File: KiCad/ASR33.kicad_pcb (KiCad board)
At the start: 2 copper layers, 42 x 35 mm, 34 parts, among them J1 USB-C, J2 Start, J3 Control, J4 Tx/Rx, U1 ESP32-WROOM-32, U2 FT231XQ, U3 NCR402U, U4 NCR402U, U5 NX6020CAKS, U6 LMR16006+FB

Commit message: Reworked
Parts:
- removed J4: Tx/Rx, RevK:Molex_MiniSPOX_H4RA
- removed the R9 at (134.6, 129.3)
- removed the U5 at (134.6, 132.0)
- added C5: NF, RevK:C_0603, F.Cu at (145.0, 132.0)
- added Q1: NX7002AK, Package_TO_SOT_SMD:SOT-23, F.Cu at (140.5, 132.0)
- added U6: QR, RevK:QR-ASR33, B.Cu at (123.0, 113.0)
- J2: value Start -> Control; footprint RevK:Molex_MiniSPOX_H2RA -> RevK:Molex_MiniSPOX_H3RA
- J3: value Control -> Teletype; footprint RevK:Molex_MiniSPOX_H3RA -> RevK:Molex_MiniSPOX_H6RA
- moved U4 7.40 mm to (131.0, 132.0)
- moved J3 6.35 mm to (141.2, 136.4)
- moved D2 4.20 mm to (152.0, 132.0)
- moved U3 4.20 mm to (135.0, 132.0)
- moved D3 4.00 mm to (148.0, 132.0)
- moved R9 2.00 mm to (143.4, 132.0), turned to 90 degrees
- moved J2 1.30 mm to (155.0, 136.4)
- renumbered C5 to C6, C6 to C7, C7 to C8, R11 to R9, U6 to U5
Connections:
- D2 pad 3: MOTOR -> POWER
- D2 pad 6: POWER -> MOTOR
- D3 pad 3: RX20MA -> START
- D3 pad 6: START -> RX20MA
- J2 pad 2: START -> POWER
- J3 pad 2: POWER -> START
- J3 pad 3: MOTOR -> Net-(J3-Pad3)
- U1 pad 23: unconnected-(U1-Pad23) -> USB
- U1 pad 24: unconnected-(U1-Pad24) -> CHARGER
- U1 pad 26: TX20MA -> START
- U1 pad 27: RX20MA -> TX20MA
- U1 pad 28: USB -> RX20MA
- U1 pad 29: CHARGER -> unconnected-(U1-Pad29)
- U1 pad 30: MOTOR -> unconnected-(U1-Pad30)
- U1 pad 31: POWER -> unconnected-(U1-Pad31)
- U1 pad 36: unconnected-(U1-Pad36) -> POWER
- U1 pad 37: START -> MOTOR
- U3 pad 2: Net-(R9-Pad1) -> Net-(J3-Pad3)
- U3 pad 3: Net-(R9-Pad1) -> Net-(J3-Pad3)
- U3 pad 5: Net-(R9-Pad1) -> Net-(J3-Pad3)
- U4 pad 2: Net-(J4-Pad4) -> Net-(J3-Pad5)
- U4 pad 3: Net-(J4-Pad4) -> Net-(J3-Pad5)
- U4 pad 5: Net-(J4-Pad4) -> Net-(J3-Pad5)
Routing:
- net Net-(J3-Pad5): track 0.00 -> 24.3 mm
- net Net-(J3-Pad3): track 0.00 -> 14.9 mm
- net Net-(J4-Pad4): track 12.4 -> 0.00 mm
- net MOTOR: track 26.7 -> 15.0 mm
- net START: track 15.0 -> 25.2 mm
- net Net-(R9-Pad1): track 9.04 -> 0.00 mm
- net CHARGER: track 16.1 -> 8.31 mm, vias 2 -> 0
- net GND: track 17.5 -> 22.7 mm, vias 9 -> 8
- net Net-(J3-Pad4): track 0.00 -> 5.03 mm
- net USB: track 14.1 -> 9.14 mm, vias 2 -> 0
- net TX20MA: track 9.33 -> 5.21 mm
- net Net-(J4-Pad2): track 3.96 -> 0.00 mm
- net GPIO0: track 14.7 -> 17.2 mm
- net Net-(R9-Pad2): track 2.28 -> 0.00 mm
- net +3V3: track 75.0 -> 76.8 mm, vias 4 -> 5
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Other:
- board text added: "MTR"
- board text added: "PWR"
- board text added: "RUN"
- board text added: "RX<"
- board text added: "RX>"
- board text added: "TX<"
- board text added: "TX>"
- board text removed: "+"
- board text removed: "-"
- board text removed: "Motor"
- board text removed: "Power"
- board text removed: "Rx"
- board text removed: "Start"
- board text removed: "Tx"

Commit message: Tweak, added button
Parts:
- added SW1: SW_Push, RevK:SW_PUSH_6mm_PTH, F.Cu at (130.5, 117.3)
- moved R10 3.00 mm to (119.0, 125.1)
- moved R8 3.00 mm to (119.0, 122.0)
- moved U5 0.78 mm to (121.8, 119.8)
- moved R9 0.30 mm to (143.7, 132.0)
- moved C5 0.20 mm to (145.2, 132.0)
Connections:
- U1 pad 16: unconnected-(U1-Pad16) -> BUTTON
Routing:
- net BUTTON: track 0.00 -> 10.8 mm
- net +3V3: track 76.8 -> 86.2 mm, vias 5 -> 4
- net O: track 27.6 -> 30.1 mm
- net EN: track 36.1 -> 38.2 mm
- net GPIO0: track 17.2 -> 18.9 mm
- net Net-(R10-Pad2): track 3.61 -> 4.71 mm
- net I: track 23.4 -> 24.1 mm
- net RX20MA: track 27.0 -> 27.6 mm
- net USB: track 9.14 -> 8.64 mm
- net GND: track 22.7 -> 22.8 mm, vias 8 -> 7
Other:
- board text added: "Power 3.3V"
- board text added: "Teletype 20mA"
- board text added: "USB-C"

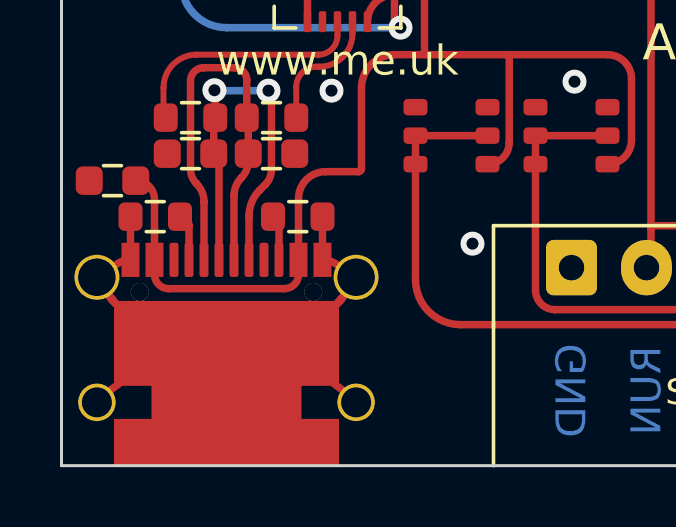
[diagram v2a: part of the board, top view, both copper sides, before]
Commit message: Correct pos for regulator
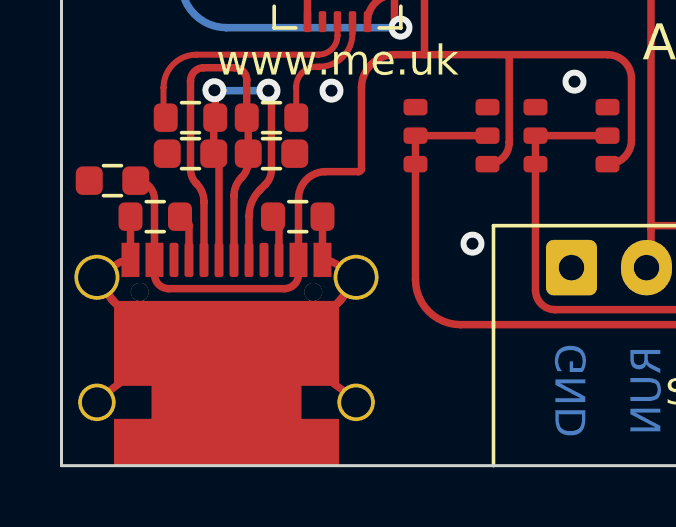
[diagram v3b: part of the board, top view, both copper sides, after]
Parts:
- moved D4 0.79 mm to (125.0, 117.5)
- moved C6 0.79 mm to (122.0, 121.9)
- moved C8 0.78 mm to (125.3, 114.4)
- moved L1 0.78 mm to (121.8, 115.9)
- moved C7 0.77 mm to (125.3, 120.7)
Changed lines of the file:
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@@
       (primitives
     (gr_arc (start 2.89 -3.045) (mid 0 -0.155) (end -2.89 -3.045) (width 0.25))
-    (gr_arc (start 4.294753 -3.49127) (mid -0.020907 -1.02625) (end -4.315692 -3.527464) (width 0.25))
+    (gr_arc (start 4.294753 -3.49127) (mid -0.016568 -1.026234) (end -4.311371 -3.519937) (width 0.25))
     (gr_arc (start -3.2 -2.485) (mid -4.015 -3.3) (end -3.2 -4.115) (width 0.25))
     (gr_arc (start 3.2 -4.115) (mid 4.015 -3.3) (end 3.2 -2.485) (width 0.25))
-    (gr_arc (start -4.32 0.635) (mid 0 -1.154403) (end 4.32 0.635) (width 0.25))
+    (gr_arc (start -4.32 0.635) (mid -0.000001 -1.154403) (end 4.319999 0.634999) (width 0.25))
         (gr_poly (pts
             (xy 3.75 0.085)
@@
   )
   (footprint "RevK:Hidden" (layer "F.Cu")
-    (at 125.95 121.14 180)
+    (at 125.35 120.65 180)
     (property "Note" "0603 or 0805")
     (property "Part No" "")
@@
   )
   (footprint "RevK:Hidden" (layer "F.Cu")
-    (at 125.95 114.9 180)
+    (at 125.35 114.4 180)
     (property "Note" "0603 or 0805")
     (property "Part No" "")
@@
   )
   (footprint "RevK:Hidden" (layer "F.Cu")
-    (at 125.57 118.02 90)
+    (at 124.96 117.52 90)
     (property "Manufacturer" "Bourns")
     (property "Note" "")
@@
   )
   (footprint "RevK:Hidden" (layer "F.Cu")
-    (at 122.4 116.4 90)
+    (at 121.8 115.9 90)
     (property "Manufacturer" "Laird")
     (property "Note" "")
@@
   )
   (footprint "RevK:Hidden" (layer "F.Cu")
-    (at 122.65 122.41)
+    (at 122.05 121.9)
     (property "Note" "X7R or X5R 0603")
     (property "Part No" "")

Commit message: Gold lettering
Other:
- board text added: "Control (3.3V)"
- board text added: "Teletype (20mA)"
- board text removed: "Power 3.3V"
- board text removed: "Teletype 20mA"
- board text removed: "USB-C"
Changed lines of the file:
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@@
     )
   )
-  (property "DATE" "2022-01-24")
+  (property "DATE" "2022-01-26")
   (net 0 "")
   (net 1 "D+")
@@
       (primitives
     (gr_arc (start 2.89 -3.045) (mid 0 -0.155) (end -2.89 -3.045) (width 0.25))
-    (gr_arc (start 4.294753 -3.49127) (mid -0.016568 -1.026234) (end -4.311371 -3.519937) (width 0.25))
+    (gr_arc (start 4.294753 -3.49127) (mid -0.012228 -1.026222) (end -4.307036 -3.512417) (width 0.25))
     (gr_arc (start -3.2 -2.485) (mid -4.015 -3.3) (end -3.2 -4.115) (width 0.25))
     (gr_arc (start 3.2 -4.115) (mid 4.015 -3.3) (end 3.2 -2.485) (width 0.25))
@@
       (effects (font (size 1 1) (thickness 0.15)))
     )
-    (fp_text value "FT231XQ" (at 0 3.3) (layer "F.Fab")
-      (effects (font (size 1 1) (thickness 0.15)))
+    (fp_text value "FT231XQ" (at 0 1.4) (layer "F.Fab")
+      (effects (font (size 0.5 0.5) (thickness 0.08)))
     )
     (fp_text user "${REFERENCE}" (at 0 0) (layer "F.Fab")
@@
       (effects (font (size 1 1) (thickness 0.15)))
     )
-    (fp_text value "ESP32-WROOM-32" (at 0 11.5 -90) (layer "F.Fab")
+    (fp_text value "ESP32-WROOM-32" (at 0.3 -8.165 -90) (layer "F.Fab")
       (effects (font (size 1 1) (thickness 0.15)))
     )
@@
       (effects (font (size 1 1) (thickness 0.15)))
     )
-    (fp_text value "NCR402U" (at 0 -2.5 unlocked) (layer "F.Fab")
-      (effects (font (size 1 1) (thickness 0.15)))
+    (fp_text value "NCR402U" (at 0 0 unlocked) (layer "F.Fab")
+      (effects (font (size 0.5 0.5) (thickness 0.08)))
     )
     (fp_line (start 0.975 1.65) (end 0.975 1.4125) (layer "F.CrtYd") (width 0.1))
@@
       (effects (font (size 1 1) (thickness 0.15)))
     )
-    (fp_text value "NCR402U" (at 0 -2.5 unlocked) (layer "F.Fab")
-      (effects (font (size 1 1) (thickness 0.15)))
+    (fp_text value "NCR402U" (at 0 0 unlocked) (layer "F.Fab")
+      (effects (font (size 0.5 0.5) (thickness 0.08)))
     )
     (fp_line (start -0.975 1.65) (end -0.975 1.4125) (layer "F.CrtYd") (width 0.1))
@@
     )
     (fp_text value "BAV99S" (at 0 2 180) (layer "F.Fab")
-      (effects (font (size 1 1) (thickness 0.15)))
+      (effects (font (size 0.5 0.5) (thickness 0.08)))
     )
     (fp_text user "${REFERENCE}" (at 0 0 90) (layer "F.Fab")
@@
     )
     (fp_text value "NX7002AK" (at 0 2.4) (layer "F.Fab")
-      (effects (font (size 1 1) (thickness 0.15)))
+      (effects (font (size 0.5 0.5) (thickness 0.08)))
     )
     (fp_text user "${REFERENCE}" (at 0 0) (layer "F.Fab")
@@
       (effects (font (size 1 1) (thickness 0.15)))
     )
-    (fp_text value "SW_Push" (at 0.5 4.45 90) (layer "F.Fab")
-      (effects (font (size 1 1) (thickness 0.15)))
+    (fp_text value "SW_Push" (at 0.1 2.6 90) (layer "F.Fab")
+      (effects (font (size 0.5 0.5) (thickness 0.08)))
     )
     (fp_text user "${REFERENCE}" (at 0 0 90) (layer "F.Fab")
@@
     )
     (fp_text value "BAV99S" (at 0 2 180) (layer "F.Fab")
-      (effects (font (size 1 1) (thickness 0.15)))
+      (effects (font (size 0.5 0.5) (thickness 0.08)))
     )
     (fp_text user "${REFERENCE}" (at 0 0 90) (layer "F.Fab")
@@
       (effects (font (size 0.5 0.5) (thickness 0.08)))
     )
-    (fp_text value "LMR16006+FB" (at -1.96 -2.55 90) (layer "F.Fab")
+    (fp_text value "LMR16006+FB" (at 6 -2.5 90) (layer "F.Fab")
       (effects (font (size 0.5 0.5) (thickness 0.1)) (justify right))
     )
-    (fp_text user "${REFERENCE}" (at 6.15 -2.55 90) (layer "F.Fab")
+    (fp_text user "${REFERENCE}" (at 6.8 -3.1 180) (layer "F.Fab")
       (effects (font (size 0.5 0.5) (thickness 0.1)) (justify left))
     )
@@
     (effects (font (size 1 1) (thickness 0.2)) (justify mirror))
   )
-  (gr_text "Teletype 20mA" (at 141.25 133.75) (layer "B.SilkS")
-    (effects (font (size 1 1) (thickness 0.15)) (justify mirror))
+  (gr_text "Teletype (20mA)" (at 141.25 134) (layer "B.SilkS")
+    (effects (font (size 0.8 0.8) (thickness 0.1)) (justify mirror))
   )
   (gr_text "ASR33\nController" (at 141.2 118.5) (layer "B.SilkS")
     (effects (font (size 1.5 1.5) (thickness 0.2)) (justify mirror))
   )
-  (gr_text "USB-C" (at 123.5 134) (layer "B.SilkS")
-    (effects (font (size 1 1) (thickness 0.15)) (justify mirror))
-  )
-  (gr_text "Power 3.3V" (at 155 133.75) (layer "B.SilkS")
-    (effects (font (size 1 1) (thickness 0.15)) (justify mirror))
+  (gr_text "Control (3.3V)" (at 155 134) (layer "B.SilkS")
+    (effects (font (size 0.8 0.8) (thickness 0.1)) (justify mirror))
   )
   (gr_text "ASR33 Controller" (at 144.4 128.9) (layer "F.SilkS")
@@
     (effects (font (size 1 1) (thickness 0.15)))
   )
-  (gr_text "GND" (at 133.9 128.9) (layer "F.Fab")
-    (effects (font (size 1 1) (thickness 0.15)))
+  (gr_text "GND" (at 135 140.5 90) (layer "B.Mask")
+    (effects (font (size 1 1) (thickness 0.24)) (justify mirror))
+  )
+  (gr_text "MTR" (at 157.5 140.5 90) (layer "B.Mask")
+    (effects (font (size 1 1) (thickness 0.24)) (justify mirror))
+  )
+  (gr_text "TX<" (at 142.5 140.5 90) (layer "B.Mask")
+    (effects (font (size 1 1) (thickness 0.24)) (justify mirror))
+  )
+  (gr_text "RX>" (at 145 140.5 90) (layer "B.Mask")
+    (effects (font (size 1 1) (thickness 0.24)) (justify mirror))
+  )
+  (gr_text "RX<" (at 147.5 140.5 90) (layer "B.Mask")
+    (effects (font (size 1 1) (thickness 0.24)) (justify mirror))
+  )
+  (gr_text "TX>" (at 140 140.5 90) (layer "B.Mask")
+    (effects (font (size 1 1) (thickness 0.24)) (justify mirror))
+  )
+  (gr_text "GND" (at 152.5 140.5 90) (layer "B.Mask")
+    (effects (font (size 1 1) (thickness 0.24)) (justify mirror))
+  )
+  (gr_text "PWR" (at 155 140.5 90) (layer "B.Mask")
+    (effects (font (size 1 1) (thickness 0.24)) (justify mirror))
+  )
+  (gr_text "RUN" (at 137.5 140.5 90) (layer "B.Mask")
+    (effects (font (size 1 1) (thickness 0.24)) (justify mirror))
   )
   (gr_text "Ext Power" (at 135.8 124.6 -90) (layer "F.Fab")
@@
   (segment (start 151.62 116.88) (end 151.62 109) (width 0.25) (layer "F.Cu") (net 4))
   (segment (start 121.35 114.9) (end 118.4 114.9) (width 0.25) (layer "F.Cu") (net 4))
-  (segment (start 121.4 108.6) (end 118.7 108.6) (width 0.25) (layer "F.Cu") (net 4))
+  (segment (start 121.6 110.125) (end 121.6 109) (width 0.25) (layer "F.Cu") (net 4))
   (segment (start 147.05 132) (end 148 132) (width 0.25) (layer "F.Cu") (net 4))
-  (segment (start 121.6 110.125) (end 121.6 108.8) (width 0.25) (layer "F.Cu") (net 4))
+  (segment (start 118.4 109.1) (end 118.4 114.9) (width 0.25) (layer "F.Cu") (net 4))
   (segment (start 150.2 117.8) (end 150.7 117.8) (width 0.25) (layer "F.Cu") (net 4))
   (segment (start 151.05 132) (end 152 132) (width 0.25) (layer "F.Cu") (net 4))
   (segment (start 128.8 111.8) (end 130.658579 111.8) (width 0.25) (layer "F.Cu") (net 4))
   (segment (start 124.4 114.4) (end 125.727208 113.072792) (width 0.25) (layer "F.Cu") (net 4))
-  (segment (start 118.4 108.9) (end 118.4 114.9) (width 0.25) (layer "F.Cu") (net 4))
   (segment (start 152 132) (end 152.95 132) (width 0.25) (layer "F.Cu") (net 4))
+  (segment (start 121.2 108.6) (end 118.9 108.6) (width 0.25) (layer "F.Cu") (net 4))
   (segment (start 148 132) (end 148.95 132) (width 0.25) (layer "F.Cu") (net 4))
   (via (at 152 132) (size 0.8) (drill 0.4) (layers "F.Cu" "B.Cu") (net 4))
@@
   (arc (start 150.7 117.8) (mid 151.350538 117.530538) (end 151.62 116.88) (width 0.25) (layer "F.Cu") (net 4))
   (arc (start 125.727208 113.072792) (mid 127.137016 112.130788) (end 128.8 111.8) (width 0.25) (layer "F.Cu") (net 4))
-  (arc (start 118.7 108.6) (mid 118.487868 108.687868) (end 118.4 108.9) (width 0.25) (layer "F.Cu") (net 4))
+  (arc (start 121.6 109) (mid 121.482843 108.717157) (end 121.2 108.6) (width 0.25) (layer "F.Cu") (net 4))
+  (arc (start 118.9 108.6) (mid 118.546447 108.746447) (end 118.4 109.1) (width 0.25) (layer "F.Cu") (net 4))
   (arc (start 121.85 114.4) (mid 121.703553 114.753553) (end 121.35 114.9) (width 0.25) (layer "F.Cu") (net 4))
-  (arc (start 121.6 108.8) (mid 121.541421 108.658579) (end 121.4 108.6) (width 0.25) (layer "F.Cu") (net 4))
   (arc (start 130.658579 111.8) (mid 130.789235 111.825989) (end 130.9 111.9) (width 0.25) (layer "F.Cu") (net 4))
   (arc (start 118.4 120.575) (mid 118.575736 120.999264) (end 119 121.175) (width 0.25) (layer "F.Cu") (net 4))

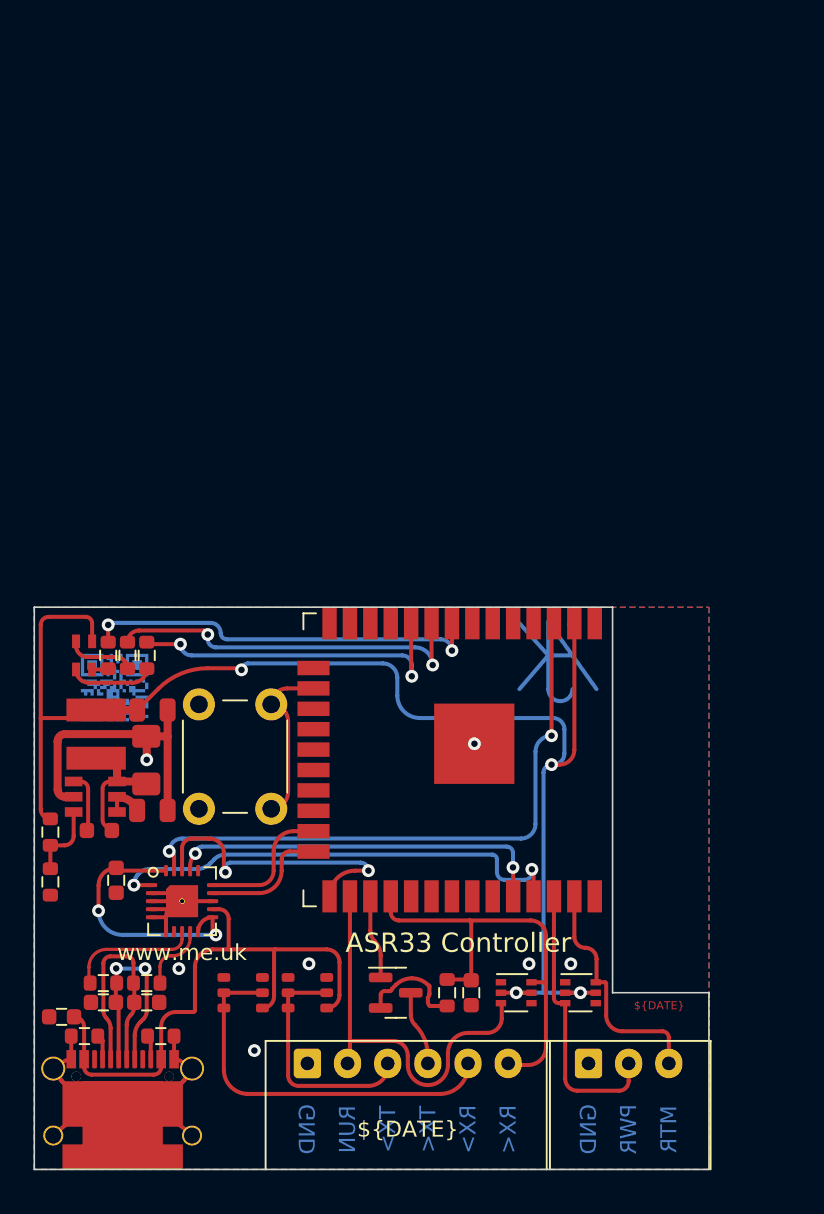
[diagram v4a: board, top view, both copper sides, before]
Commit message: Reworkd tx/rx
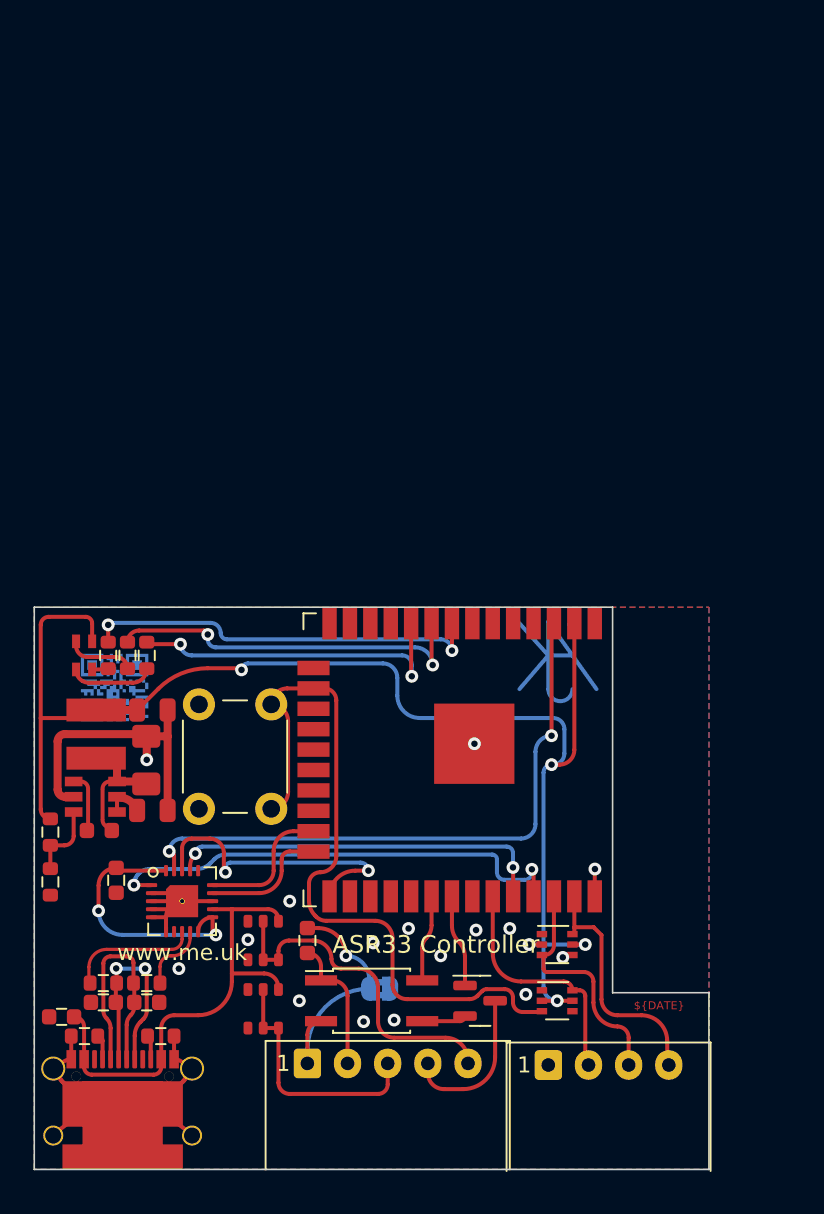
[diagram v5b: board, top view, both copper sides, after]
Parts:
- removed the R9 at (143.7, 132.0)
- added JP1: Rx-RTN, Jumper:SolderJumper-2_P1.3mm_Bridged2Bar_RoundedPad1.0x1.5mm, B.Cu at (139.5, 131.8)
- added U6: LTV-355T, Package_SO:SO-4_4.4x3.6mm_P2.54mm, F.Cu at (139.0, 132.5)
- J2: value Control -> Conn_01x04; footprint RevK:Molex_MiniSPOX_H3RA -> RevK:Molex_MiniSPOX_H4RA
- J3: value Teletype -> Conn_01x05; footprint RevK:Molex_MiniSPOX_H6RA -> RevK:Molex_MiniSPOX_H5RA
- moved C8 10.7 mm to (135.0, 128.8), turned to -90 degrees
- moved Q1 5.27 mm to (145.8, 132.5)
- moved U3 4.26 mm to (132.2, 128.8), turned to 90 degrees
- moved D2 3.33 mm to (150.6, 129.0)
- moved D3 2.60 mm to (150.6, 132.5)
- moved U4 1.60 mm to (132.2, 133.0), turned to 90 degrees
- moved J2 1.25 mm to (153.8, 136.5)
- moved J3 1.25 mm to (140.0, 136.4)
- renumbered C6 to C5, C7 to C6, C8 to C7, C5 to C8, R10 to R9, U6 to U7
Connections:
- C8 pad 1: GND -> Net-(C8-Pad1)
- C8 pad 2: RX20MA -> Net-(C8-Pad2)
- D2 pad 3: POWER -> MOTOR
- D2 pad 6: MOTOR -> POWER
- D3 pad 3: START -> BUTTON
- D3 pad 6: RX20MA -> START
- J2 pad 2: POWER -> START
- J3 pad 1: GND -> Net-(C8-Pad1)
- J3 pad 2: START -> Net-(C8-Pad2)
- U1 pad 26: START -> unconnected-(U1-Pad26)
- U1 pad 27: TX20MA -> unconnected-(U1-Pad27)
- U1 pad 28: RX20MA -> unconnected-(U1-Pad28)
- U1 pad 30: unconnected-(U1-Pad30) -> RX20MA
- U1 pad 31: unconnected-(U1-Pad31) -> TX20MA
- U1 pad 33: unconnected-(U1-Pad33) -> START
- U1 pad 36: POWER -> MOTOR
- U1 pad 37: MOTOR -> POWER
- U3 pad 2: Net-(J3-Pad3) -> Net-(J3-Pad5)
- U3 pad 3: Net-(J3-Pad3) -> Net-(J3-Pad5)
- U3 pad 5: Net-(J3-Pad3) -> Net-(J3-Pad5)
- U4 pad 2: Net-(J3-Pad5) -> Net-(J3-Pad3)
- U4 pad 3: Net-(J3-Pad5) -> Net-(J3-Pad3)
- U4 pad 5: Net-(J3-Pad5) -> Net-(J3-Pad3)
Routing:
- net BUTTON: track 10.8 -> 46.3 mm
- net RX20MA: track 27.6 -> 5.38 mm
- net Net-(C8-Pad1): track 0.00 -> 15.9 mm, vias 0 -> 1
- net START: track 25.2 -> 15.1 mm
- net Net-(C8-Pad2): track 0.00 -> 8.52 mm
- net VBUS: track 37.2 -> 29.7 mm
- net Net-(J3-Pad4): track 4.67 -> 9.89 mm
- net Net-(J3-Pad5): track 24.3 -> 21.2 mm
- net POWER: track 17.7 -> 15.3 mm
- net GND: track 22.8 -> 21.3 mm, vias 7 -> 16
- net Net-(J3-Pad3): track 14.9 -> 15.5 mm
- net TX20MA: track 5.21 -> 5.75 mm
- net +3V3: track 86.0 -> 86.2 mm, vias 4 -> 5
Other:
- board text removed: "GND"
- board text removed: "MTR"
- board text removed: "PWR"
- board text removed: "RUN"
- board text removed: "RX<"
- board text removed: "RX>"
- board text removed: "TX<"
- board text removed: "TX>"

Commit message: Reworked PCB and manuals
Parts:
- JP1: footprint Jumper:SolderJumper-2_P1.3mm_Bridged2Bar_RoundedPad1.0x1.5mm -> RevK:SolderJumper-2_P1.3mm_Bridged2Bar_RoundedPad1.0x1.5mm
- moved J2 0.10 mm to (153.8, 136.4)
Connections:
- net MOTOR renamed MTR
- net POWER renamed PWR
- net START renamed RUN
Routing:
- net TX20MA: track 5.75 -> 6.49 mm
- net BUTTON: track 46.3 -> 45.7 mm
- net GND: vias 16 -> 14
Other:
- board text added: "MTR"
- board text added: "PWR"
- board text added: "RUN"
- board text added: "RX<"
- board text added: "RX>"
- board text added: "RX⏚"
- board text added: "TX<"
- board text added: "TX>"
- board text added: "⏚"
